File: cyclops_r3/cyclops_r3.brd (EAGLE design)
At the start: 124.5 x 79.9 mm, 91 parts, among them Q1 BC817, Q2 IRF540, U1 MCP4921, U2 317-N, U3 TLV3701, U4 337-N, U5 ADR03, U6 OP1177, U7 LTC2052, U8 ZXTD45

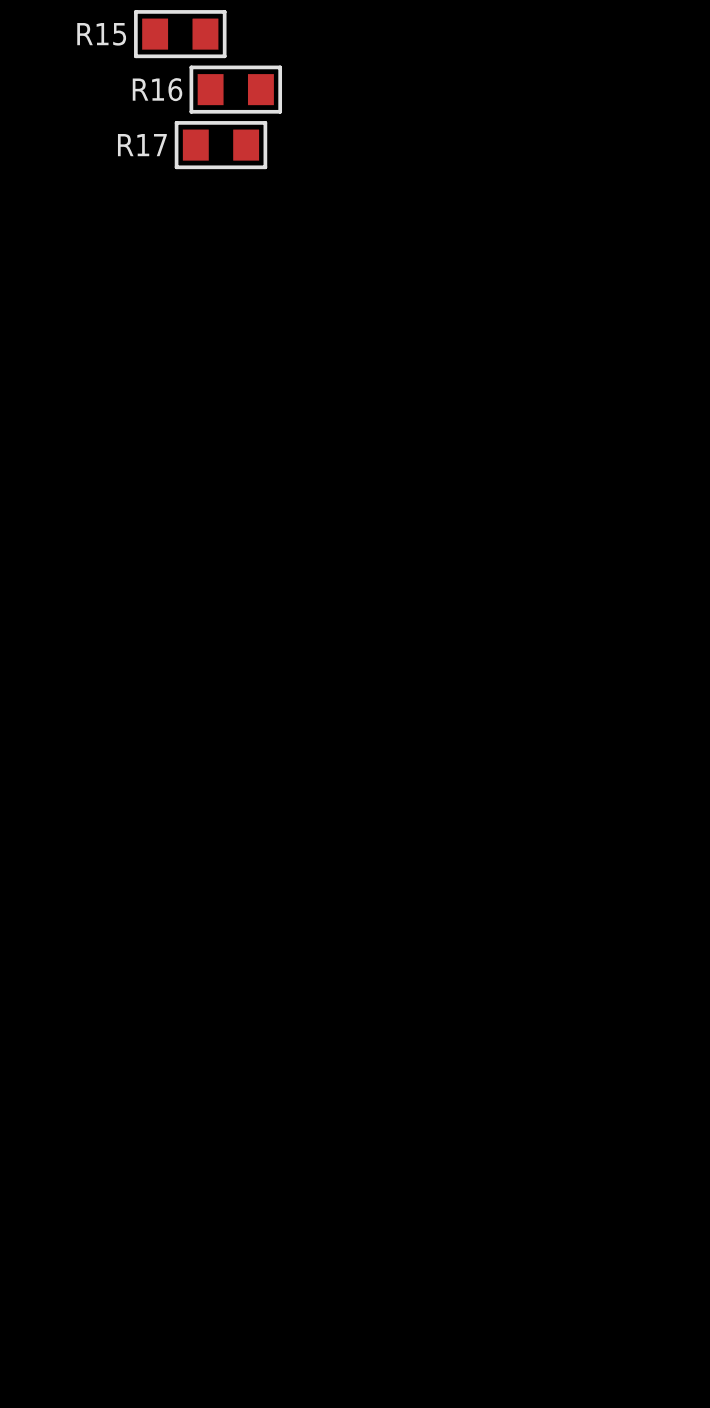
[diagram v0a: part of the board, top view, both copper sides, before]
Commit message: Modified the board to incorporate most of the improvements frr3.3. Need to test optical feedback.
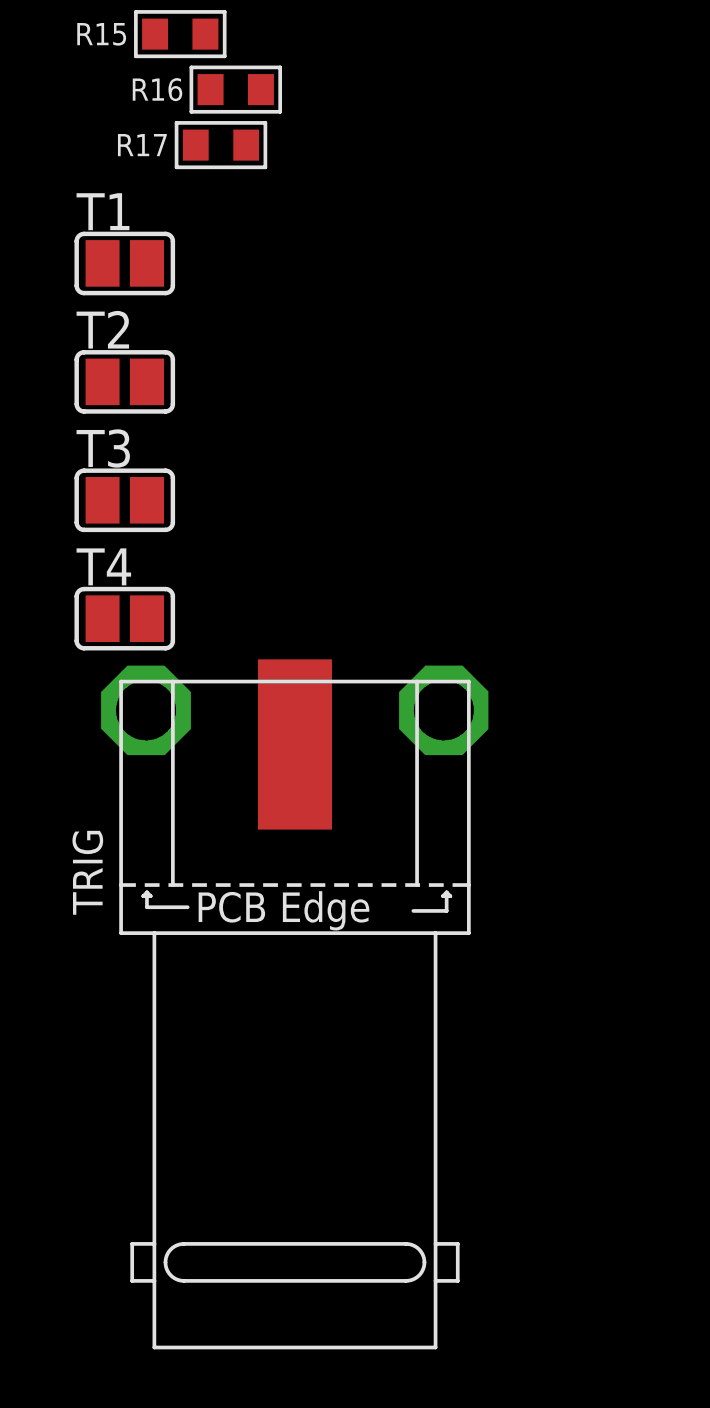
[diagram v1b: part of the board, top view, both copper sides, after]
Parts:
- added T1, T2, T3, T4: (no value), cyclops:SJ
- added TRIG: 361V509E, cyclops:361V509E
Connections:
- new net CS7: ARDUNIO.D10, ARDUNIO.D7, ARDUNIO.D8, ARDUNIO.D9, T1.2, T2.2, T3.2, T4.2
- new net GND2: TRIG.2, TRIG.3
- new net TRIG: T1.1, T2.1, T3.1, T4.1, TRIG.1
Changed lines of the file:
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@@
 <attribute name="MPN" value="ERJ-3EKFxxxxV" x="-8.128" y="-17.78" size="1.778" layer="27" display="off"/>
 </element>
+<element name="T1" library="cyclops" package="SJ" value="" x="-11.43" y="-21.844"/>
+<element name="T2" library="cyclops" package="SJ" value="" x="-11.43" y="-25.908"/>
+<element name="T3" library="cyclops" package="SJ" value="" x="-11.43" y="-29.972"/>
+<element name="T4" library="cyclops" package="SJ" value="" x="-11.43" y="-34.036"/>
+<element name="TRIG" library="cyclops" package="361V509E" value="361V509E" x="-5.588" y="-43.18"/>
 </elements>
 <signals>
@@
 <contactref element="R15" pad="2"/>
 </signal>
+<signal name="TRIG">
+<contactref element="T1" pad="1"/>
+<contactref element="T2" pad="1"/>
+<contactref element="T3" pad="1"/>
+<contactref element="T4" pad="1"/>
+<contactref element="TRIG" pad="1"/>
+<wire x1="-12.192" y1="-29.972" x2="-12.192" y2="-34.036" width="0" layer="19" extent="1-1"/>
+<wire x1="-12.192" y1="-25.908" x2="-12.192" y2="-29.972" width="0" layer="19" extent="1-1"/>
+<wire x1="-12.192" y1="-21.844" x2="-12.192" y2="-25.908" width="0" layer="19" extent="1-1"/>
+<wire x1="-5.588" y1="-38.354" x2="-12.192" y2="-34.036" width="0" layer="19" extent="1-1"/>
+</signal>
+<signal name="CS7">
+<contactref element="T4" pad="2"/>
+<contactref element="T3" pad="2"/>
+<contactref element="T2" pad="2"/>
+<contactref element="T1" pad="2"/>
+<contactref element="ARDUNIO" pad="D7"/>
+<contactref element="ARDUNIO" pad="D8"/>
+<contactref element="ARDUNIO" pad="D9"/>
+<contactref element="ARDUNIO" pad="D10"/>
+<wire x1="6.724" y1="41.656" x2="6.724" y2="45.72" width="0" layer="19" extent="1-1"/>
+<wire x1="6.724" y1="39.116" x2="6.724" y2="41.656" width="0" layer="19" extent="1-1"/>
+<wire x1="6.724" y1="36.576" x2="6.724" y2="39.116" width="0" layer="19" extent="1-1"/>
+<wire x1="-10.668" y1="-21.844" x2="6.724" y2="36.576" width="0" layer="19" extent="1-1"/>
+<wire x1="-10.668" y1="-25.908" x2="-10.668" y2="-21.844" width="0" layer="19" extent="1-1"/>
+<wire x1="-10.668" y1="-29.972" x2="-10.668" y2="-25.908" width="0" layer="19" extent="1-1"/>
+<wire x1="-10.668" y1="-34.036" x2="-10.668" y2="-29.972" width="0" layer="19" extent="1-1"/>
+</signal>
+<signal name="GND2">
+<contactref element="TRIG" pad="3"/>
+<contactref element="TRIG" pad="2"/>
+<wire x1="-0.47625" y1="-37.1856" x2="-10.69975" y2="-37.1856" width="0" layer="19" extent="1-1"/>
+</signal>
 </signals>

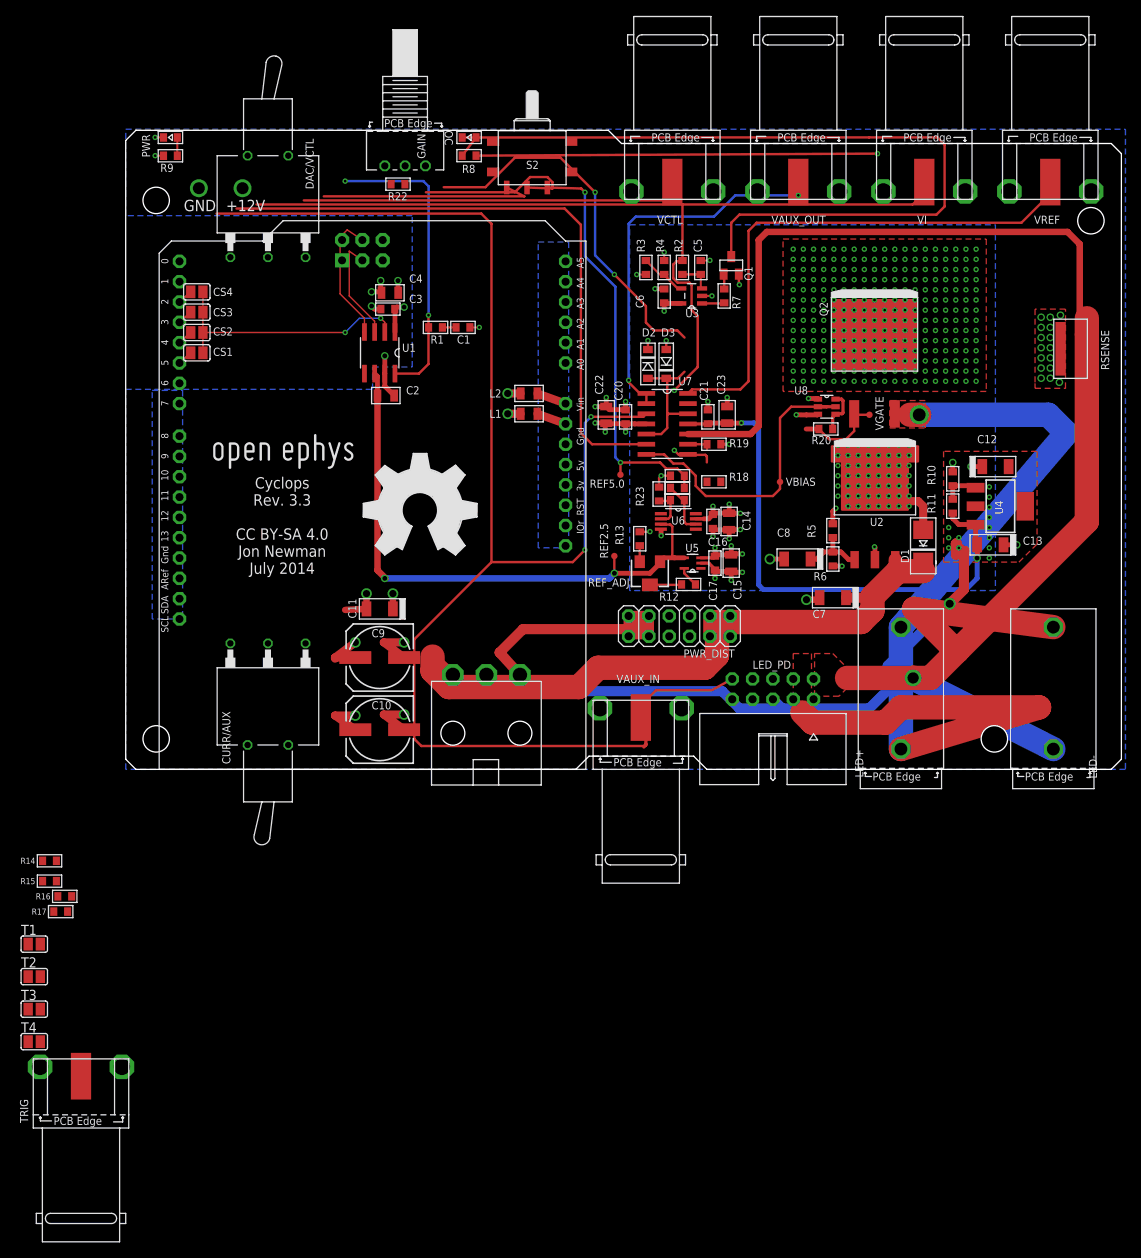
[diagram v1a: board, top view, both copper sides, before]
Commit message: More revisions to 3.3.
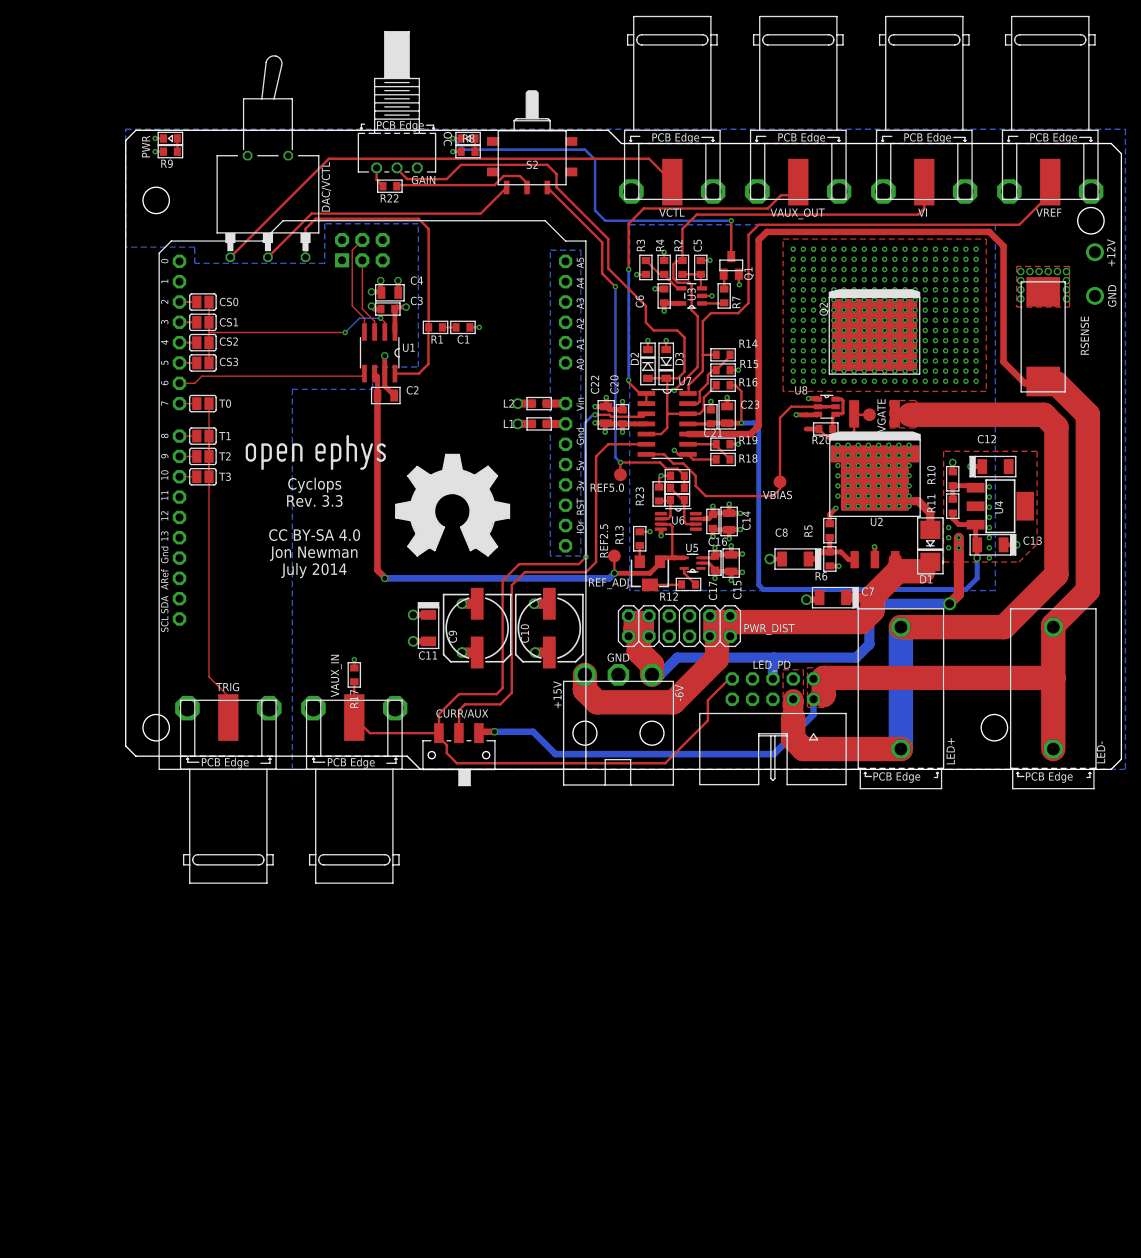
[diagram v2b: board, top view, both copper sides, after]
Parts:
- removed CS4, T4: (no value), cyclops:SJ
- added CS0, T0: (no value), cyclops:SJ
- CURR/AUX: device cyclops:2M1-SP1-T2-B4-M6RE -> cyclops:JS102011SAQN
- L1, L2: device cyclops:0805 -> cyclops:0603
- REF2.5, REF5.0, VBIAS, VGATE: value TPTP08R -> TPTP16R; device cyclops:TP08R -> cyclops:TP16R
- RSENSE: value 0.5,1W -> 0.5,3W; device cyclops:2512W -> cyclops:PWR5322
- moved R15 105.7 mm to (74.7, 49.9)
- moved R14 105.3 mm to (74.7, 51.8), turned to 180 degrees
- moved R16 104.2 mm to (74.7, 48.0), turned to 180 degrees
- moved T3 69.8 mm to (9.65, 36.6), turned to 180 degrees
- moved T2 68.4 mm to (9.65, 39.1), turned to 180 degrees
- moved T1 66.9 mm to (9.65, 41.7), turned to 180 degrees
- moved TRIG 48.5 mm to (12.8, 1.65)
- moved R17 47.1 mm to (28.6, 11.8), turned to 90 degrees
- moved VAUX_IN 35.8 mm to (28.6, 1.65)
- moved C10 24.7 mm to (53.0, 17.7), turned to 270 degrees
- moved CURR/AUX 23.9 mm to (41.7, 1.78), turned to 0 degrees
- moved PWR_IN 16.5 mm to (57.4, 4.52)
- moved C9 12.7 mm to (43.9, 17.7), turned to 270 degrees
- moved RSENSE 7.90 mm to (114.7, 59.7)
- moved C11 6.56 mm to (37.9, 17.7), turned to 270 degrees
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- renumbered ARDUNIO to LEONARDO
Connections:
- removed net CS7: LEONARDO.D10, LEONARDO.D7, LEONARDO.D8, LEONARDO.D9, T1.2, T2.2, T3.2, T4.2
- removed net GND1: R15.2
- removed net GND2: TRIG.2, TRIG.3
- removed net VI1: R14.2
- new net T0: LEONARDO.D7, T0.2
- new net T1: LEONARDO.D8, T1.2
- new net T2: LEONARDO.D9, T2.2
- new net T3: LEONARDO.D10, T3.2
- net -6V: now also LED_PD.5; no longer LED_PD.6
- net CS: now also CS0.2; no longer CS4.2
- net CS0: now also CS0.1; no longer CS4.1
- net CS1: now also CS1.1; no longer CS3.1
- net CS3: now also CS3.1; no longer CS1.1
- net GND: now also LED_PD.6, R15.2, TRIG.2, TRIG.3; no longer LED_PD.5
- net LED-: now also CURR/AUX.3; no longer CURR/AUX.1
- net TRIG: now also T0.1; no longer T4.1
- net VAUX: now also CURR/AUX.1; no longer CURR/AUX.3
- net VREF: now also R14.2
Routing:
- net VAUX: track 186.9 -> 122.7 mm
- net +12V: track 109.0 -> 53.7 mm, vias 343 -> 344
- net VI: track 125.9 -> 72.2 mm
- net N$9: track 100.2 -> 48.3 mm, vias 0 -> 2
- net TRIG: track 0.00 -> 45.3 mm
- net -6V: track 114.2 -> 78.5 mm
- net LED+: track 118.6 -> 93.7 mm, vias 1 -> 0
- net LDAC: track 0.08 -> 23.7 mm
- net VFB: track 78.7 -> 55.7 mm
- net +15V: track 91.3 -> 70.1 mm
- net LED-: track 198.9 -> 216.9 mm
- net _VREF: track 63.5 -> 77.5 mm, vias 2 -> 0
- net VINPUT: track 48.0 -> 61.6 mm
- net GND: track 76.0 -> 66.1 mm, vias 55 -> 52
- net N$8: track 0.00 -> 9.22 mm
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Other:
- outline, holes or cut-outs redrawn
- board text added: "+15V"
- board text added: "-6V"

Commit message: Finished up BOM for revision 3.3. Also fixed up spice simulation.
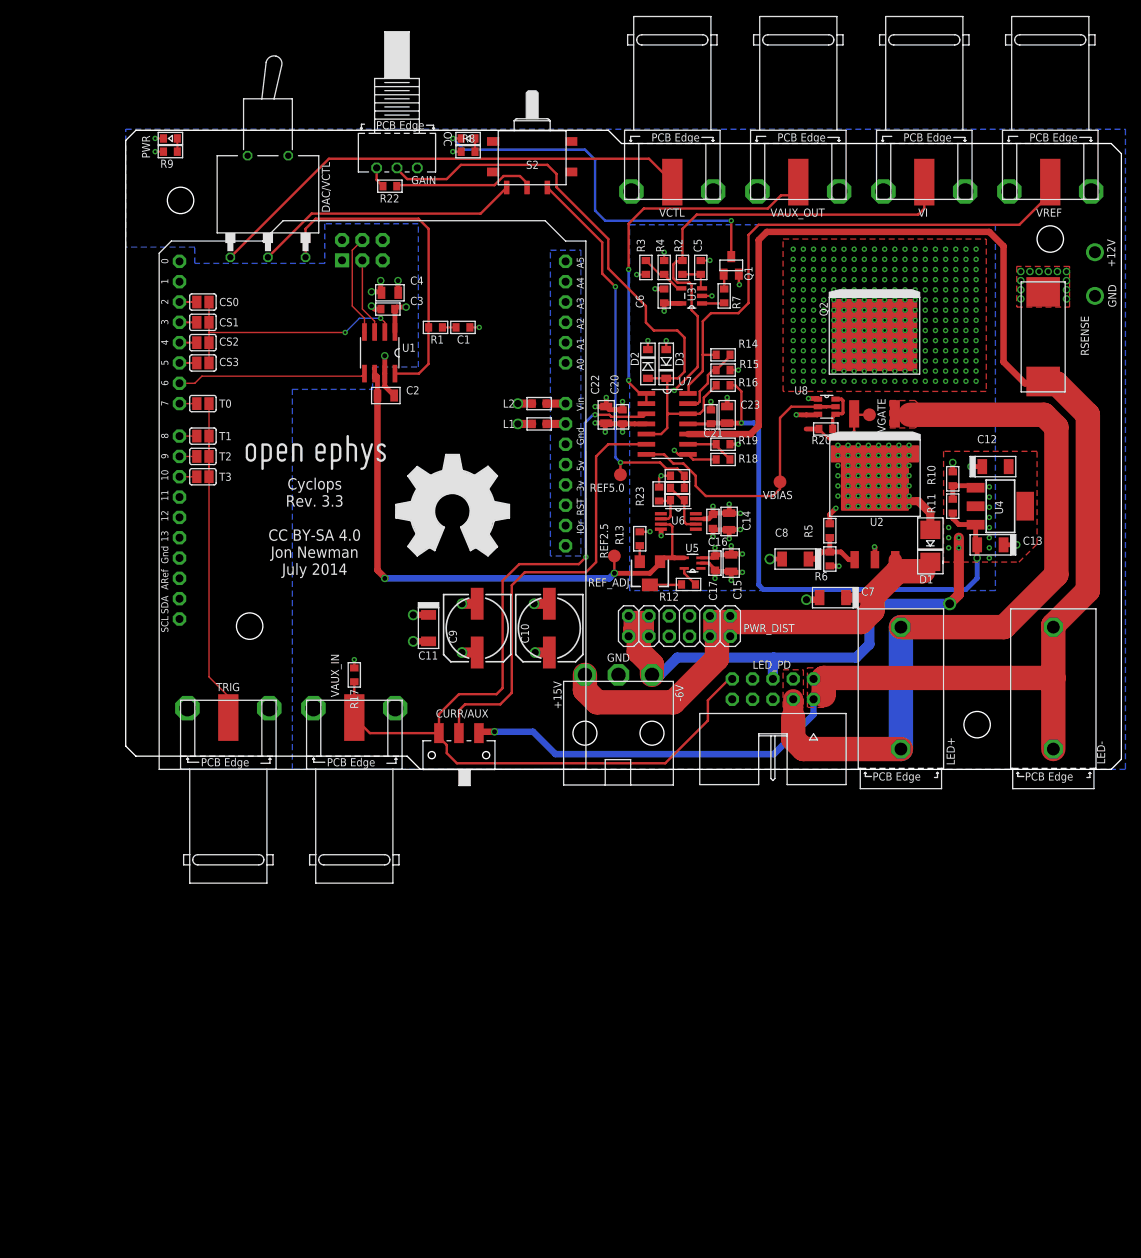
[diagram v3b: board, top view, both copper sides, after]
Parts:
- Q2: value IRF540 -> IRF510
